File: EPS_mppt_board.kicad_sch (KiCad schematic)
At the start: 0 parts

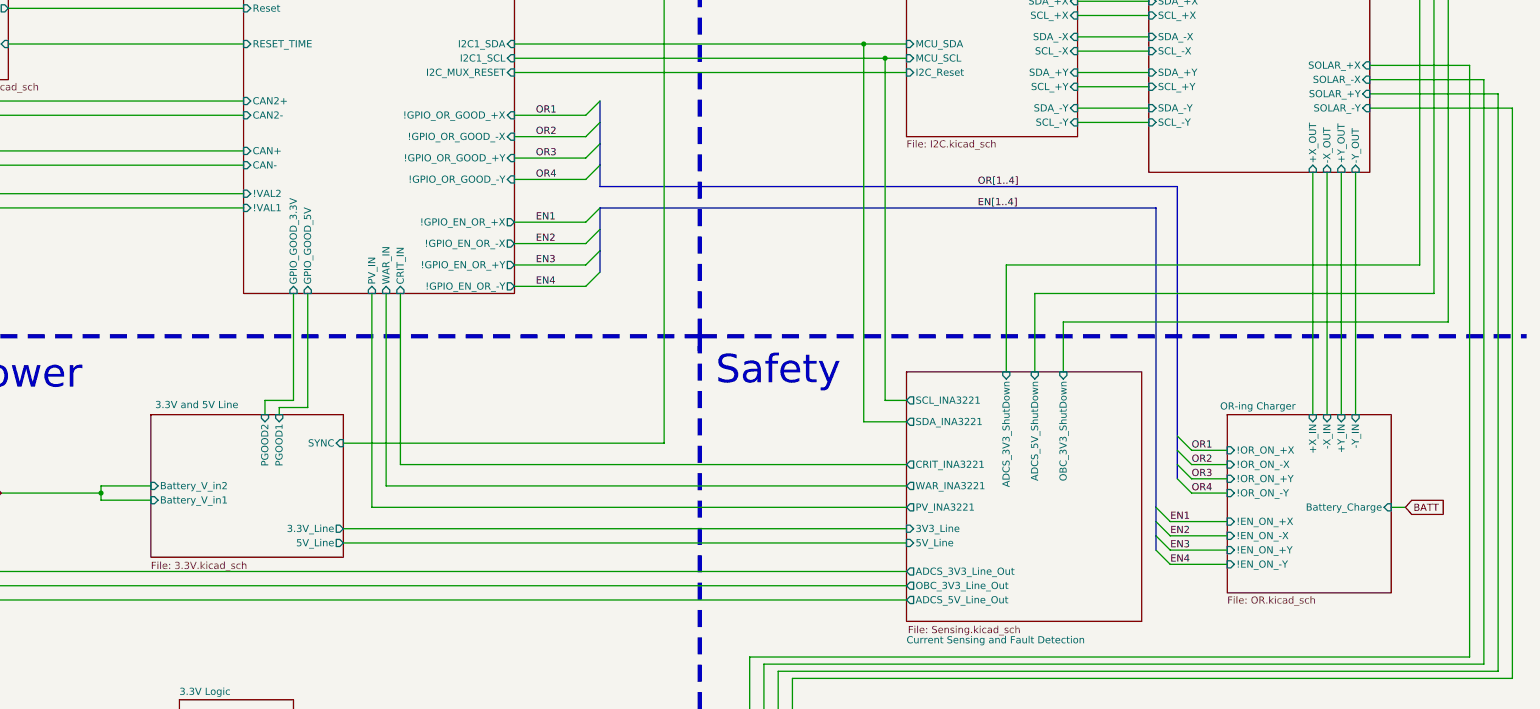
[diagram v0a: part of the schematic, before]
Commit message: LTC4162 layout almost done
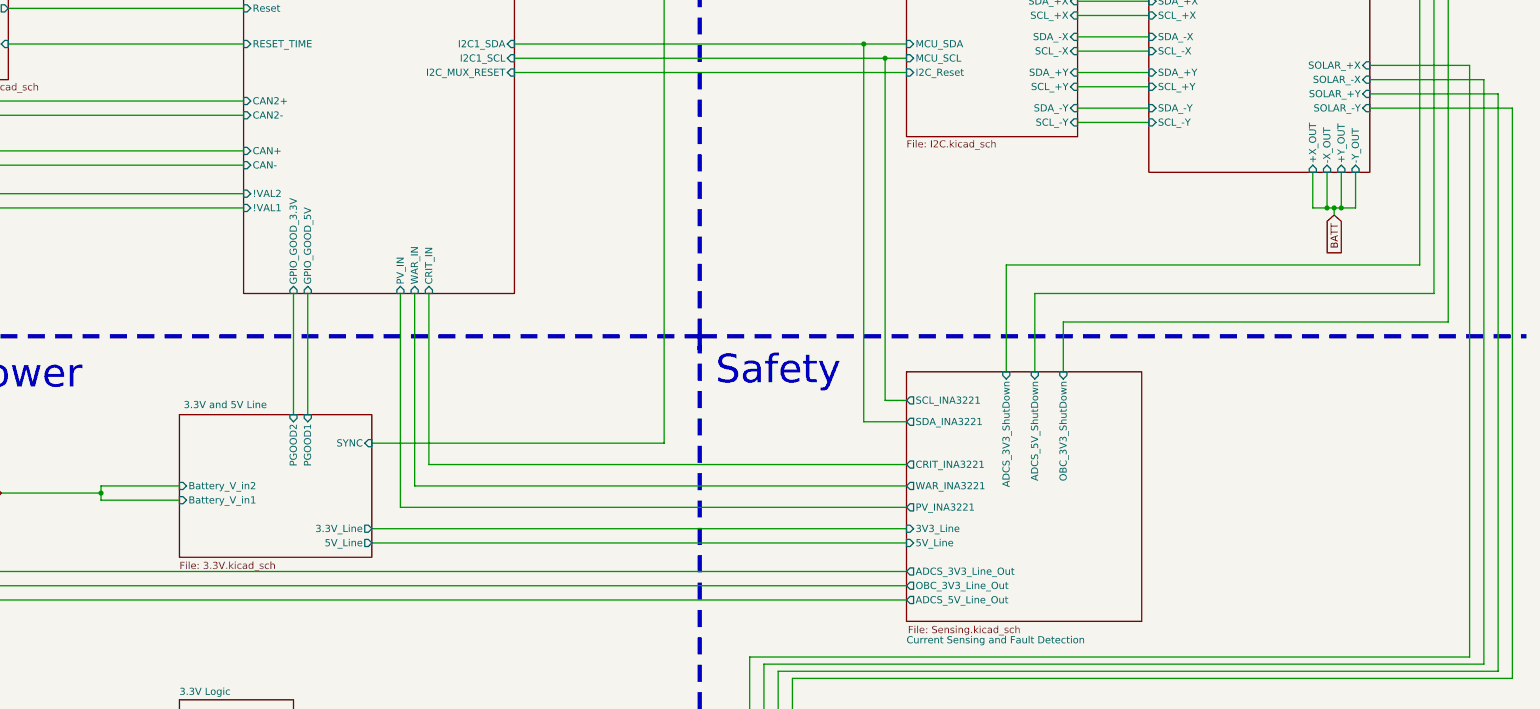
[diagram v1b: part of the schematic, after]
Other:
- removed sheet OR-ing Charger
- sheet STM32L4 ports: added none; removed !GPIO_EN_OR_+X, !GPIO_EN_OR_+Y, !GPIO_EN_OR_-X, !GPIO_EN_OR_-Y, !GPIO_OR_GOOD_+X, !GPIO_OR_GOOD_+Y, !GPIO_OR_GOOD_-X, !GPIO_OR_GOOD_-Y
